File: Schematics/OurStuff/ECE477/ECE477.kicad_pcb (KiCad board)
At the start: 2 copper layers, 67 parts, among them J1 USB_B_Micro, J2 Barrel_Jack, J3 OLED JST PH 7pin, J7 D30V30F3, Q1 SS8050-G, Q2 SS8050-G, U1 ESP32-WROOM-32E, U2 CP2102N-Axx-xQFN28

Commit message: started routing 💢
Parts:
- removed TP10: IO0, TestPoint:TestPoint_Keystone_5010-5014_Multipurpose
- removed TP9: EN, TestPoint:TestPoint_Keystone_5010-5014_Multipurpose
- moved RST1 113.8 mm to (120.8, 80.5)
- moved Boot1 113.2 mm to (120.8, 72.5)
- moved H2 103.9 mm to (186.5, 53.0)
- moved H3 103.0 mm to (186.5, 75.5)
- moved TP3 101.4 mm to (168.5, 52.5)
- moved C1 93.7 mm to (59.9, 169.0)
- moved C2 93.7 mm to (59.9, 172.0)
- moved C3 93.7 mm to (59.9, 175.0)
- moved C4 93.7 mm to (59.9, 178.0)
- moved C6 93.7 mm to (59.9, 181.1)
- moved C7 93.7 mm to (59.9, 184.1)
- moved C8 93.7 mm to (59.9, 187.1)
- moved C9 93.7 mm to (59.9, 190.1)
- moved D4 93.7 mm to (64.9, 151.3)
- moved D5 93.7 mm to (64.9, 154.4)
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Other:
- board outline added: 90 x 40.5 mm

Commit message: finished pcb layout v1
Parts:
- C4, C6, C7, C8, C9, D1, D10, D11, D2, D3, R1, R10, R11, R12, R14, R15, R16, R2, R3, R4, R8, R9: moved to B.Cu
- moved C9 183.3 mm to (181.0, 52.5), turned to 180 degrees
- moved C8 173.3 mm to (169.0, 52.5)
- moved R12 154.3 mm to (182.0, 66.0), turned to 180 degrees
- moved C2 153.0 mm to (164.8, 60.6)
- moved C1 153.0 mm to (164.8, 57.6)
- moved R7 149.4 mm to (173.9, 69.9), turned to -90 degrees
- moved R9 147.5 mm to (162.0, 63.5), turned to 180 degrees
- moved C6 146.6 mm to (172.5, 87.2), turned to -90 degrees
- moved C7 146.2 mm to (169.5, 87.3), turned to -90 degrees
- moved R6 146.0 mm to (169.0, 65.9)
- moved R11 145.7 mm to (173.5, 66.0)
- moved D9 145.2 mm to (177.0, 74.1)
- moved R18 141.1 mm to (176.9, 78.0)
- moved R2 138.0 mm to (140.8, 54.0), turned to 180 degrees
- moved D8 137.7 mm to (169.7, 74.1)
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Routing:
- net GND: track 0.00 -> 284.9 mm, vias 0 -> 5
- net +3.3V: track 0.00 -> 182.6 mm, vias 0 -> 4
- net /EN: track 0.00 -> 87.4 mm, vias 0 -> 2
- net /Button2: track 0.00 -> 84.7 mm, vias 0 -> 3
- net Vbat: track 0.00 -> 77.7 mm
- net /Button1: track 0.00 -> 58.0 mm, vias 0 -> 3
- net /IO0: track 0.00 -> 39.6 mm, vias 0 -> 1
- net Net-(U2-RXD): track 0.00 -> 37.0 mm, vias 0 -> 2
- net Net-(U2-TXD): track 0.00 -> 30.9 mm, vias 0 -> 2
- net BAT_ADC: track 0.00 -> 27.1 mm, vias 0 -> 1
- net Net-(U2-VBUS): track 0.00 -> 26.8 mm, vias 0 -> 1
- net /TX: track 0.00 -> 26.0 mm
- net /O_DIN: track 0.00 -> 25.2 mm, vias 0 -> 4
- net /Mic_In: track 0.00 -> 24.5 mm
- net /RX: track 0.00 -> 23.9 mm
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
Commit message: pre deletion
pre deleted ver in case of misshap
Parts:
- moved D1 1.30 mm to (160.7, 56.1)
- moved D2 0.88 mm to (160.6, 60.7)
- moved D3 0.36 mm to (160.8, 58.4)
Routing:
- net GND: track 284.9 -> 286.8 mm
- net V_BUS: track 22.9 -> 22.2 mm
- net /USB_DP: track 10.7 -> 11.4 mm
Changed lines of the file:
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@@
 		(tags "capacitor handsolder")
 		(property "Reference" "C2"
-			(at 0.0075 -1.46 0)
+			(at 1.0875 1.82 0)
 			(layer "F.SilkS")
 			(effects
 				(font
-					(size 0.508 0.508)
+					(size 1 1)
 					(thickness 0.127)
 				)
@@
 			(effects
 				(font
-					(size 0.508 0.508)
+					(size 1 1)
 					(thickness 0.127)
 				)
@@
 	(footprint "Diode_SMD:D_SOD-923"
 		(layer "B.Cu")
-		(at 160.53 59.85 180)
+		(at 160.64 60.72 180)
 		(descr "https://www.onsemi.com/pub/Collateral/ESD9B-D.PDF#page=4")
 		(tags "Diode SOD923")
 		(property "Reference" "D2"
-			(at -1.7 -0.03 0)
+			(at -0.13 1.1 0)
 			(layer "B.SilkS")
 			(effects
 				(font
-					(size 0.762 0.762)
+					(size 1 1)
 					(thickness 0.15)
 				)
@@
 	(footprint "Diode_SMD:D_SOD-923"
 		(layer "B.Cu")
-		(at 160.53 57.35 180)
+		(at 160.7075 56.06 180)
 		(descr "https://www.onsemi.com/pub/Collateral/ESD9B-D.PDF#page=4")
 		(tags "Diode SOD923")
 		(property "Reference" "D1"
-			(at -1.62 -0.01 0)
+			(at -0.07 1.12 0)
 			(layer "B.SilkS")
 			(effects
 				(font
-					(size 0.762 0.762)
+					(size 1 1)
 					(thickness 0.15)
 				)
@@
 	(footprint "Diode_SMD:D_SOD-923"
 		(layer "B.Cu")
-		(at 160.93 58.69 180)
+		(at 160.76 58.37 180)
 		(descr "https://www.onsemi.com/pub/Collateral/ESD9B-D.PDF#page=4")
 		(tags "Diode SOD923")
 		(property "Reference" "D3"
-			(at -1.43 -0.11 0)
+			(at -0.13 1.14 0)
 			(layer "B.SilkS")
 			(effects
 				(font
-					(size 0.508 0.508)
+					(size 1 1)
 					(thickness 0.127)
 				)
@@
 	)
 	(segment
+		(start 159.193398 60.053398)
+		(end 159.193398 60.883398)
+		(width 0.254)
+		(layer "F.Cu")
+		(net 2)
+	)
+	(segment
 		(start 150.43 89.43)
 		(end 156.75 83.11)
@@
 	)
 	(segment
+		(start 159.193398 60.883398)
+		(end 160.01 61.7)
+		(width 0.254)
+		(layer "F.Cu")
+		(net 2)
+	)
+	(segment
 		(start 176 63.75)
 		(end 175 62.75)
@@
 	)
 	(segment
-		(start 160.1 60.96)
-		(end 160.035 60.895)
-		(width 0.254)
-		(layer "F.Cu")
-		(net 2)
-	)
-	(segment
 		(start 173.94 72.15)
 		(end 175.93 74.14)
@@
 		(net 2)
 	)
-	(segment
-		(start 159.193398 60.053398)
-		(end 160.035 60.895)
-		(width 0.254)
-		(layer "F.Cu")
-		(net 2)
-	)
 	(via
 		(at 164.64 53.75)
@@
 	)
 	(via
-		(at 160.035 60.895)
+		(at 140.56 78.22)
 		(size 0.6)
 		(drill 0.3)
@@
 	)
 	(via
-		(at 140.56 78.22)
+		(at 160.01 61.7)
 		(size 0.6)
 		(drill 0.3)
@@
 	)
 	(segment
+		(start 166.852 51.448)
+		(end 164.64 53.66)
+		(width 0.254)
+		(layer "B.Cu")
+		(net 2)
+	)
+	(segment
 		(start 131.675 61.605)
 		(end 139.23 54.05)
@@
 	)
 	(segment
+		(start 161.18 56.1125)
+		(end 161.1275 56.06)
+		(width 0.254)
+		(layer "B.Cu")
+		(net 2)
+	)
+	(segment
 		(start 180.58 55.5)
 		(end 179.925 54.845)
@@
 	)
 	(segment
-		(start 160.035 60.895)
-		(end 160.035 60.765)
+		(start 161.14 56.07)
+		(end 162.32 56.07)
 		(width 0.254)
 		(layer "B.Cu")
@@
 	)
 	(segment
+		(start 160.99 60.72)
+		(end 160.01 61.7)
+		(width 0.254)
+		(layer "B.Cu")
+		(net 2)
+	)
+	(segment
 		(start 140.56 88.42)
 		(end 140.56 78.22)
@@
 	)
 	(segment
-		(start 160.94 58.28)
-		(end 160.94 57.36)
+		(start 161.18 58.37)
+		(end 161.18 60.6)
 		(width 0.254)
 		(layer "B.Cu")
@@
 	)
 	(segment
-		(start 135.744072 59.767)
-		(end 135.413 59.435928)
+		(start 161.18 60.6)
+		(end 161.06 60.72)
 		(width 0.254)
 		(layer "B.Cu")
@@
 	)
 	(segment
-		(start 160.95 59.09)
-		(end 161.35 58.69)
+		(start 135.744072 59.767)
+		(end 135.413 59.435928)
 		(width 0.254)
 		(layer "B.Cu")
@@
 	)
 	(segment
+		(start 162.32 56.07)
+		(end 164.64 53.75)
+		(width 0.254)
+		(layer "B.Cu")
+		(net 2)
+	)
+	(segment
 		(start 131.675 64.5)
 		(end 131.675 61.605)
@@
 	)
 	(segment
-		(start 161.35 58.69)
-		(end 160.94 58.28)
+		(start 161.06 60.72)
+		(end 160.99 60.72)
 		(width 0.254)
 		(layer "B.Cu")
@@
 	)
 	(segment
-		(start 160.035 60.765)
-		(end 160.95 59.85)
+		(start 164.64 53.66)
+		(end 164.64 53.75)
 		(width 0.254)
 		(layer "B.Cu")
@@
 	)
 	(segment
-		(start 160.94 57.36)
-		(end 160.95 57.35)
+		(start 139.91 60.73)
+		(end 138.947 59.767)
 		(width 0.254)
 		(layer "B.Cu")
@@
 	)
 	(segment
-		(start 139.91 60.73)
-		(end 138.947 59.767)
+		(start 161.18 58.37)
+		(end 161.18 56.1125)
 		(width 0.254)
 		(layer "B.Cu")
@@
 	)
 	(segment
-		(start 160.95 57.35)
-		(end 166.852 51.448)
-		(width 0.254)
-		(layer "B.Cu")
-		(net 2)
-	)
-	(segment
 		(start 170.075 54.795)
 		(end 170.075 52.5)
@@
 	)
 	(segment
-		(start 160.95 59.85)
-		(end 160.95 59.09)
-		(width 0.254)
-		(layer "B.Cu")
-		(net 2)
-	)
-	(segment
 		(start 138.947 59.767)
 		(end 135.744072 59.767)
@@
 	)
 	(segment
-		(start 160.16 56.5)
+		(start 158.13 53.49)
 		(end 157.15 53.49)
 		(width 0.254)
@@
 	)
 	(segment
+		(start 159.67 55.03)
+		(end 158.13 53.49)
+		(width 0.254)
+		(layer "F.Cu")
+		(net 7)
+	)
+	(segment
 		(start 157.15 53.49)
 		(end 156.740001 53.899999)
@@
 	)
 	(via
-		(at 160.16 56.5)
+		(at 159.67 55.03)
 		(size 0.6)
 		(drill 0.3)
@@
 	)
 	(segment
-		(start 160.11 57.35)
-		(end 160.11 56.5)
+		(start 160.3 56.07)
+		(end 159.67 55.44)
 		(width 0.254)
 		(layer "B.Cu")
@@
 	)
 	(segment
-		(start 160.11 56.5)
-		(end 160.16 56.5)
+		(start 159.67 55.44)
+		(end 159.67 55.03)
 		(width 0.254)
 		(layer "B.Cu")
@@
 	)
 	(segment
-		(start 159.237253 59.426398)
-		(end 159.686398 59.426398)
+		(start 160.22 60.72)
+		(end 160.22 60.409145)
 		(width 0.2)
 		(layer "B.Cu")
@@
 	)
 	(segment
-		(start 155.85 56.039145)
-		(end 155.85 52.5)
+		(start 160.22 60.409145)
+		(end 159.237253 59.426398)
 		(width 0.2)
 		(layer "B.Cu")
@@
 	)
 	(segment
-		(start 159.237253 59.426398)
-		(end 155.85 56.039145)
+		(start 155.85 56.039145)
+		(end 155.85 52.5)
 		(width 0.2)
 		(layer "B.Cu")
@@
 	)
 	(segment
-		(start 159.686398 59.426398)
-		(end 160.11 59.85)
+		(start 159.237253 59.426398)
+		(end 155.85 56.039145)
 		(width 0.2)
 		(layer "B.Cu")
@@
 	)
 	(segment
-		(start 160.51 58.69)
-		(end 159.61 58.69)
+		(start 160.34 58.37)
+		(end 159.93 58.37)
 		(width 0.2)
 		(layer "B.Cu")
@@
 	)
 	(segment
-		(start 159.61 58.69)
+		(start 159.93 58.37)
 		(end 159.6 58.7)
 		(width 0.2)

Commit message: ver 2 before delete
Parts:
- D1, D2, D3, R15, R16, R3, R4: moved to F.Cu
- Q1, Q2, R13, R5, R6, R7: moved to B.Cu
- moved TP5 56.0 mm to (114.8, 79.0)
- moved R7 54.8 mm to (119.5, 63.0), turned to 180 degrees
- moved R6 49.9 mm to (119.5, 60.0)
- moved R15 17.3 mm to (160.0, 67.3), turned to -90 degrees
- moved R19 11.3 mm to (131.8, 79.5)
- moved R20 11.3 mm to (131.8, 86.0)
- moved TP1 11.1 mm to (119.5, 53.7)
- moved C3 10.8 mm to (131.8, 73.5)
- moved R16 10.5 mm to (150.0, 67.2), turned to -90 degrees
- moved D1 9.97 mm to (150.8, 55.5), turned to 90 degrees
- moved R3 9.85 mm to (146.2, 59.0), turned to 180 degrees
- moved D6 9.50 mm to (156.4, 67.3), turned to -90 degrees
- moved D7 9.38 mm to (153.2, 67.2), turned to -90 degrees
- moved D5 8.69 mm to (114.4, 67.6), turned to 180 degrees
- moved D3 7.72 mm to (153.5, 55.8), turned to -90 degrees
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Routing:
- net /Button2: track 84.7 -> 26.3 mm, vias 3 -> 0
- net BAT_ADC: track 27.1 -> 81.7 mm
- net Vbat: track 77.7 -> 30.7 mm
- net Net-(U2-RXD): track 37.0 -> 0.00 mm, vias 2 -> 0
- net +3.3V: track 182.6 -> 219.6 mm, vias 4 -> 3
- net /Button1: track 58.0 -> 24.3 mm, vias 3 -> 0
- net Net-(U2-TXD): track 30.9 -> 0.00 mm, vias 2 -> 0
- net /EN: track 87.4 -> 56.7 mm
- net Net-(U2-VBUS): track 26.8 -> 0.00 mm, vias 1 -> 0
- net GND: track 286.8 -> 305.7 mm, vias 5 -> 4
- net Net-(U2-~{RST}): track 22.5 -> 5.64 mm, vias 1 -> 0
- net /DTR: track 14.5 -> 29.9 mm, vias 2 -> 1
- net /Debug_3: track 17.6 -> 29.3 mm, vias 3 -> 1
- net Net-(U2-~{SUSPEND}): track 17.2 -> 6.05 mm, vias 1 -> 0
- net /O_CS: track 15.0 -> 8.24 mm, vias 2 -> 0
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
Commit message: hell yeah
pcb complete ver 1 (no more deletes please)
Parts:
- C1, C2, C3, R15: moved to B.Cu
- moved TP6 67.6 mm to (176.2, 53.2)
- moved TP5 64.7 mm to (176.2, 58.8)
- moved TP4 61.1 mm to (170.8, 53.2)
- moved R7 56.8 mm to (176.3, 66.5)
- moved R6 56.8 mm to (176.2, 63.5)
- moved R5 47.0 mm to (163.2, 52.0)
- moved R13 47.0 mm to (157.8, 52.0)
- moved RST1 46.0 mm to (162.2, 60.2), turned to 180 degrees
- moved D4 45.4 mm to (163.3, 54.5)
- moved D5 45.4 mm to (157.8, 54.4)
- moved D3 41.5 mm to (116.2, 74.1), turned to 45 degrees
- moved TP8 41.3 mm to (112.2, 75.0)
- moved J1 41.3 mm to (116.2, 68.7), turned to -45 degrees
- moved D1 40.4 mm to (113.2, 70.5), turned to 135 degrees
- moved C1 37.5 mm to (128.8, 71.2), turned to -135 degrees
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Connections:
- B1 pad 2: GND -> Gnd_Bat
- B2 pad 2: GND -> Gnd_Bat
- Boot1 pad 2: GND -> Gnd_Bat
- C1 pad 2: GND -> Gnd_Bat
- C2 pad 2: GND -> Gnd_Bat
- C3 pad 1: GND -> Gnd_Bat
- C4 pad 2: GND -> Gnd_Bat
- C6 pad 2: GND -> Gnd_Bat
- C7 pad 2: GND -> Gnd_Bat
- C8 pad 2: GND -> Gnd_Bat
- C9 pad 2: GND -> Gnd_Bat
- D1 pad 1: GND -> Gnd_Bat
- D10 pad 2: GND -> Gnd_Bat
- D11 pad 1: GND -> Gnd_Bat
- D2 pad 1: GND -> Gnd_Bat
- D3 pad 1: GND -> Gnd_Bat
- D4 pad 1: GND -> Gnd_Bat
- D5 pad 1: GND -> Gnd_Bat
- D8 pad 1: GND -> Gnd_Bat
- D9 pad 1: GND -> Gnd_Bat
- J1 pad 5: GND -> Gnd_Bat
- J3 pad 2: GND -> Gnd_Bat
- J7 pad 2: GND -> Gnd_Bat
- Microphone1 pad 2: GND -> Gnd_Bat
- R2 pad 2: GND -> Gnd_Bat
- R4 pad 1: GND -> Gnd_Bat
- R7 pad 2: GND -> Gnd_Bat
- RST1 pad 1: GND -> Gnd_Bat
- TP2 pad 1: GND -> Gnd_Bat
- TP3 pad 1: GND -> Gnd_Bat
- TP4 pad 1: GND -> Gnd_Bat
- U1 pad 1: GND -> Gnd_Bat
- U1 pad 10: /Debug_1 -> /Button1
- U1 pad 11: /Debug_2 -> /Button2
- U1 pad 15: GND -> Gnd_Bat
- U1 pad 27: /Button1 -> /Debug_2
- U1 pad 28: /Button2 -> /Debug_1
- U1 pad 38: GND -> Gnd_Bat
- U1 pad 39: GND -> Gnd_Bat
- U2 pad 29: GND -> Gnd_Bat
- U2 pad 3: GND -> Gnd_Bat
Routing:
- net GND: track 305.7 -> 0.00 mm, vias 4 -> 0
- net Vbat: track 30.7 -> 81.6 mm, vias 0 -> 2
- net BAT_ADC: track 81.7 -> 30.8 mm
- net /Button1: track 24.3 -> 54.6 mm, vias 0 -> 1
- net /Button2: track 26.3 -> 54.1 mm, vias 0 -> 1
- net +3.3V: track 219.6 -> 244.1 mm, vias 3 -> 4
- net /IO0: track 37.8 -> 62.0 mm
- net /EN: track 56.7 -> 79.2 mm, vias 2 -> 3
- net Net-(U2-RXD): track 0.00 -> 18.8 mm
- net /O_RST: track 8.16 -> 26.6 mm, vias 0 -> 1
- net /O_DIN: track 18.6 -> 37.0 mm
- net /O_CS: track 8.24 -> 26.5 mm, vias 0 -> 1
- net Net-(U2-TXD): track 0.00 -> 17.2 mm
- net /O_CLK: track 8.51 -> 23.3 mm, vias 0 -> 1
- net /O_DC: track 9.64 -> 21.6 mm
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- added copper zone on B.Cu, net Gnd_Bat
- added copper zone on F.Cu, net Gnd_Bat
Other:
- board size 90 x 40.5 mm -> 105 x 40.5 mm

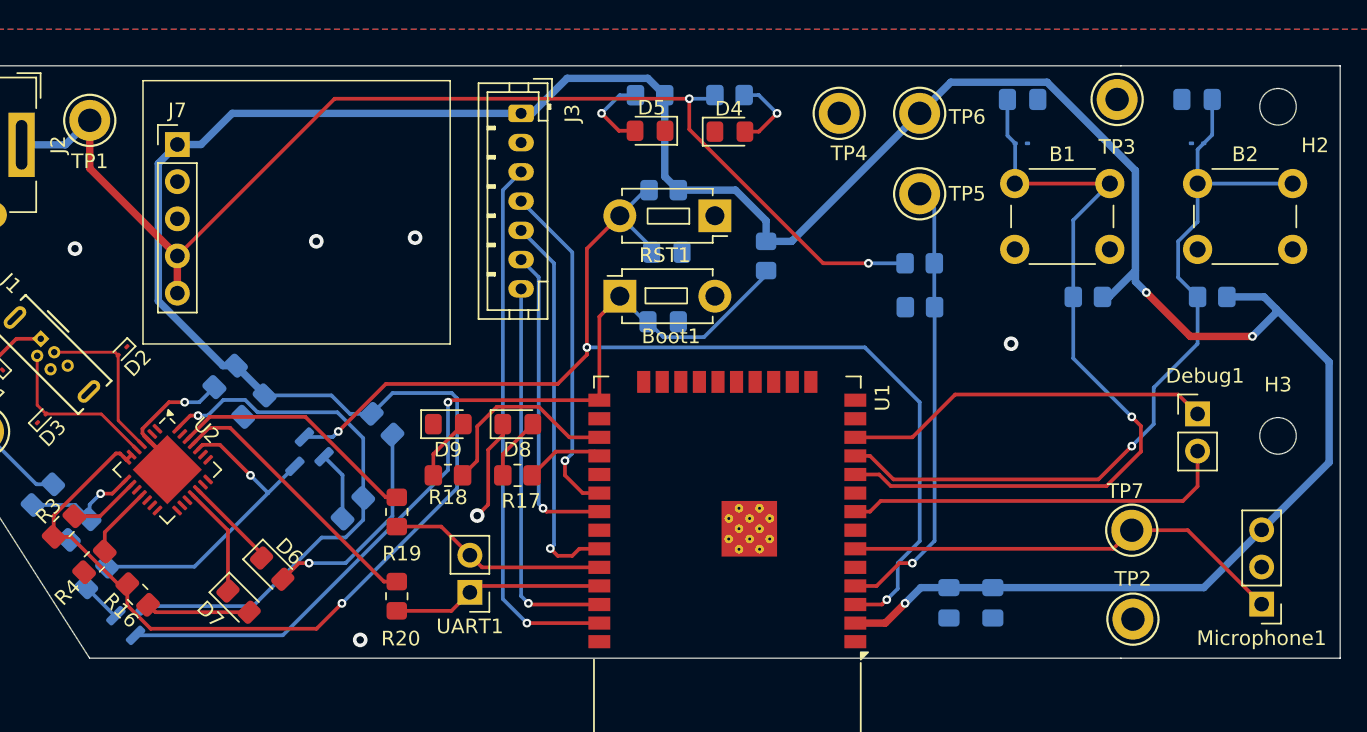
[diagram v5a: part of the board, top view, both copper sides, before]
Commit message: fixed footprints
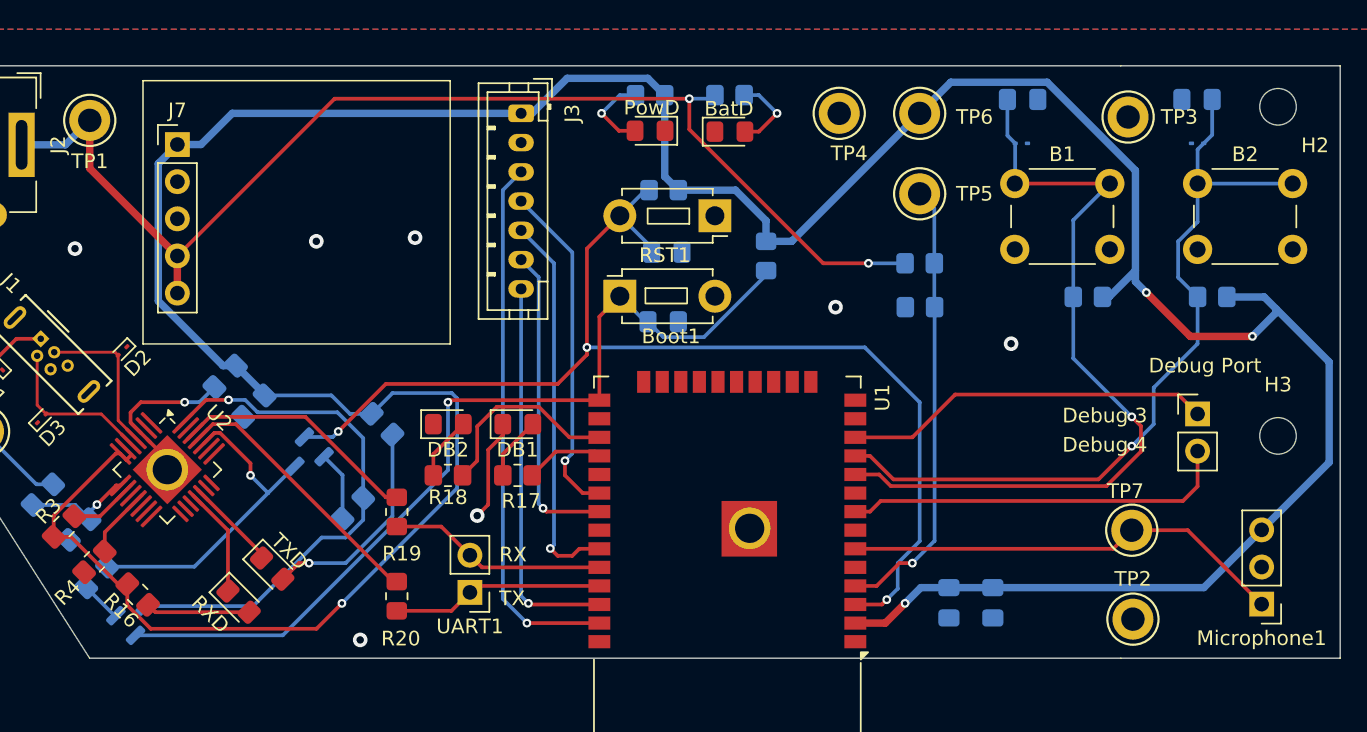
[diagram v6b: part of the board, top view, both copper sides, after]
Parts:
- Debug Port: renamed from Debug1
- moved TP3 1.42 mm to (190.5, 53.5)
- renumbered D4 to BatD, D8 to DB1, D9 to DB2, D5 to PowD, D7 to RXD, D6 to TXD
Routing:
- net Gnd_Bat: track 19.2 -> 17.8 mm, vias 8 -> 9
- net /RTS: track 22.0 -> 22.6 mm
- net Net-(U2-VBUS): track 8.54 -> 9.04 mm
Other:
- board text added: "Debug 3"
- board text added: "Debug 4"
- board text added: "RX"
- board text added: "TX"
